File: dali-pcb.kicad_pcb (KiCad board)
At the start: 2 copper layers, 180.3 x 106.7 mm, 57 parts, among them J1 12-22.5V DC, J10 LOLIN-S3 (R), J11 ESP32-S3-DEVKITC-1 (L), J12 ESP32-S3-DEVKITC-1 (R), J13 LOLIN-S2-MINI (L), J14 LOLIN-S2-MINI (R), J15 DALI BUS, J16 DALI BUS, J17 FTDI-MCU, J18 A10, J19 A5-1, J2 DALI BUS, J20 A5-2, J21 A2-1, J22 A2-2, J23 A2-3, J24 A2-4, J25 A2-5, J26 D8, J27 D4-1, J28 D4-2, J29 D2-1, J3 5V DC, J30 D2-2, J31 D2-3, J32 D2-4, J33 D1-11, J34 D1-12, J35 D1-13, J36 D1-14, J37 FTDI-DALI, J4 5V DC, J5 5V DC, J6 5V DC, J7 5V DC, J8 GND, J9 LOLIN-S3 (L), Q1 PZT2222A, Q2 MMBT2222A, U1 TCLT1000, U2 TCLT1000

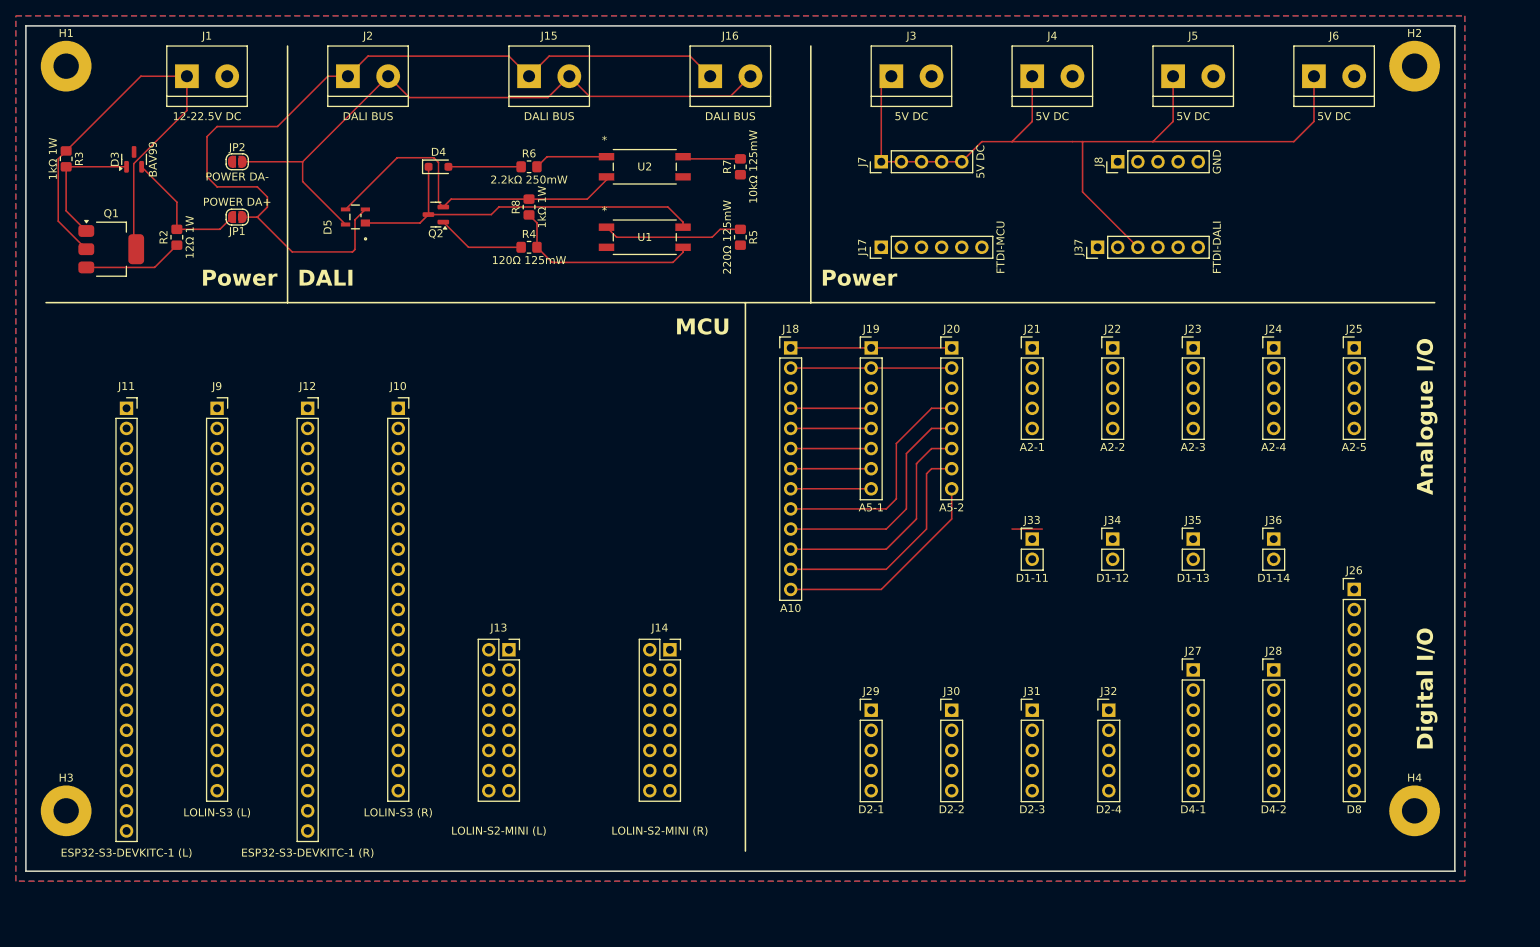
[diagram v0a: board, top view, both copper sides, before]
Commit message: Increase board size to protect the MCU USB connections
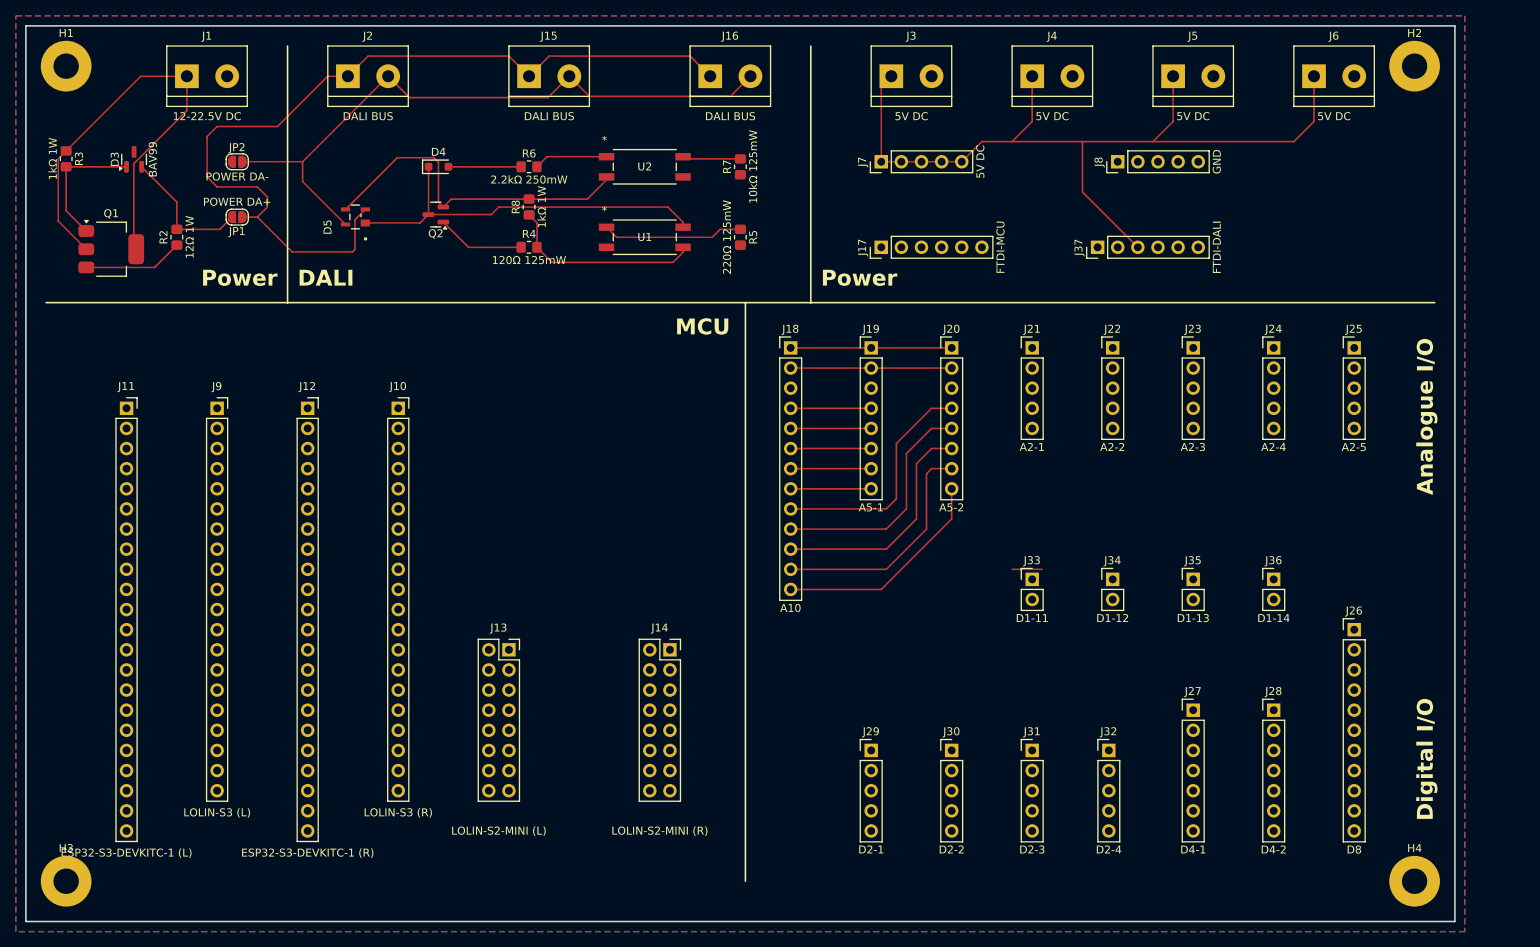
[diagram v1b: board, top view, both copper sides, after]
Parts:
- moved H3 8.89 mm to (20.3, 123.2)
- moved H4 8.89 mm to (190.5, 123.2)
- moved J29 5.08 mm to (121.9, 106.7)
- moved J30 5.08 mm to (132.1, 106.7)
- moved J31 5.08 mm to (142.2, 106.7)
- moved J32 5.08 mm to (151.9, 106.7)
- moved J26 5.08 mm to (182.9, 91.4)
- moved J27 5.08 mm to (162.6, 101.6)
- moved J28 5.08 mm to (172.7, 101.6)
- moved J33 5.08 mm to (142.2, 85.1)
- moved J34 5.08 mm to (152.4, 85.1)
- moved J35 5.08 mm to (162.6, 85.1)
- moved J36 5.08 mm to (172.7, 85.1)
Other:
- board size 180.3 x 106.7 mm -> 180.3 x 113 mm
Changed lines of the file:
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@@
 	(footprint "Connector_PinHeader_2.54mm:PinHeader_1x05_P2.54mm_Vertical"
 		(layer "F.Cu")
-		(at 151.91 101.6)
+		(at 151.91 106.68)
 		(descr "Through hole straight pin header, 1x05, 2.54mm pitch, single row")
 		(tags "Through hole pin header THT 1x05 2.54mm single row")
@@
 	(footprint "Connector_PinHeader_2.54mm:PinHeader_1x02_P2.54mm_Vertical"
 		(layer "F.Cu")
-		(at 162.56 80.01)
+		(at 162.56 85.09)
 		(descr "Through hole straight pin header, 1x02, 2.54mm pitch, single row")
 		(tags "Through hole pin header THT 1x02 2.54mm single row")
@@
 	(footprint "Connector_PinHeader_2.54mm:PinHeader_1x07_P2.54mm_Vertical"
 		(layer "F.Cu")
-		(at 162.56 96.52)
+		(at 162.56 101.6)
 		(descr "Through hole straight pin header, 1x07, 2.54mm pitch, single row")
 		(tags "Through hole pin header THT 1x07 2.54mm single row")
@@
 	(footprint "Connector_PinHeader_2.54mm:PinHeader_1x05_P2.54mm_Vertical"
 		(layer "F.Cu")
-		(at 142.24 101.6)
+		(at 142.24 106.68)
 		(descr "Through hole straight pin header, 1x05, 2.54mm pitch, single row")
 		(tags "Through hole pin header THT 1x05 2.54mm single row")
@@
 	(footprint "Connector_PinHeader_2.54mm:PinHeader_1x07_P2.54mm_Vertical"
 		(layer "F.Cu")
-		(at 172.72 96.52)
+		(at 172.72 101.6)
 		(descr "Through hole straight pin header, 1x07, 2.54mm pitch, single row")
 		(tags "Through hole pin header THT 1x07 2.54mm single row")
@@
 	(footprint "Connector_PinHeader_2.54mm:PinHeader_1x02_P2.54mm_Vertical"
 		(layer "F.Cu")
-		(at 172.72 80.01)
+		(at 172.72 85.09)
 		(descr "Through hole straight pin header, 1x02, 2.54mm pitch, single row")
 		(tags "Through hole pin header THT 1x02 2.54mm single row")
@@
 	(footprint "Connector_PinHeader_2.54mm:PinHeader_1x02_P2.54mm_Vertical"
 		(layer "F.Cu")
-		(at 142.24 80.01)
+		(at 142.24 85.09)
 		(descr "Through hole straight pin header, 1x02, 2.54mm pitch, single row")
 		(tags "Through hole pin header THT 1x02 2.54mm single row")
@@
 	(footprint "Connector_PinHeader_2.54mm:PinHeader_1x05_P2.54mm_Vertical"
 		(layer "F.Cu")
-		(at 132.08 101.6)
+		(at 132.08 106.68)
 		(descr "Through hole straight pin header, 1x05, 2.54mm pitch, single row")
 		(tags "Through hole pin header THT 1x05 2.54mm single row")
@@
 	(footprint "Connector_PinHeader_2.54mm:PinHeader_1x02_P2.54mm_Vertical"
 		(layer "F.Cu")
-		(at 152.4 80.01)
+		(at 152.4 85.09)
 		(descr "Through hole straight pin header, 1x02, 2.54mm pitch, single row")
 		(tags "Through hole pin header THT 1x02 2.54mm single row")
@@
 	(footprint "MountingHole:MountingHole_3.2mm_M3_Pad"
 		(layer "F.Cu")
-		(at 190.5 114.3)
+		(at 190.5 123.19)
 		(descr "Mounting Hole 3.2mm, M3, generated by kicad-footprint-generator mountinghole.py")
 		(tags "mountinghole M3")
@@
 	(footprint "MountingHole:MountingHole_3.2mm_M3_Pad"
 		(layer "F.Cu")
-		(at 20.32 114.3)
+		(at 20.32 123.19)
 		(descr "Mounting Hole 3.2mm, M3, generated by kicad-footprint-generator mountinghole.py")
 		(tags "mountinghole M3")
@@
 	(footprint "Connector_PinHeader_2.54mm:PinHeader_1x05_P2.54mm_Vertical"
 		(layer "F.Cu")
-		(at 121.92 101.6)
+		(at 121.92 106.68)
 		(descr "Through hole straight pin header, 1x05, 2.54mm pitch, single row")
 		(tags "Through hole pin header THT 1x05 2.54mm single row")
@@
 	(footprint "Connector_PinHeader_2.54mm:PinHeader_1x11_P2.54mm_Vertical"
 		(layer "F.Cu")
-		(at 182.88 86.36)
+		(at 182.88 91.44)
 		(descr "Through hole straight pin header, 1x11, 2.54mm pitch, single row")
 		(tags "Through hole pin header THT 1x11 2.54mm single row")
@@
 	(gr_line
 		(start 106.045 50.165)
-		(end 106.045 119.38)
+		(end 106.045 123.19)
 		(stroke
 			(width 0.2)
@@
 	(gr_rect
 		(start 15.24 15.24)
-		(end 195.58 121.92)
+		(end 195.58 128.27)
 		(stroke
 			(width 0.2)
@@
 	)
 	(gr_text "Digital I/O"
-		(at 193.04 106.68 90)
+		(at 193.04 115.57 90)
 		(layer "F.SilkS")
 		(effects
@@
 		(layer "Cmts.User")
 		(pts
+			(xy 27.94 118.17) (xy 27.94 128.27)
+		)
+		(height -19.05)
+		(orientation 1)
+		(format
+			(prefix "")
+			(suffix "")
+			(units 2)
+			(units_format 1)
+			(precision 4)
+			(suppress_zeroes yes)
+		)
+		(style
+			(thickness 0.1)
+			(arrow_length 1.27)
+			(text_position_mode 0)
+			(arrow_direction outward)
+			(extension_height 0.58642)
+			(extension_offset 0.5)
+			(keep_text_aligned yes)
+		)
+		(gr_text "10.1 mm"
+			(at 7.79 123.22 90)
+			(layer "Cmts.User")
+			(effects
+				(font
+					(size 1 1)
+					(thickness 0.1)
+				)
+			)
+		)
+	)
+	(dimension
+		(type orthogonal)
+		(layer "Cmts.User")
+		(pts
 			(xy 62.23 111.76) (xy 73.66 111.76)
 		)
@@
 	)
 	(segment
-		(start 143.51 78.74)
-		(end 139.7 78.74)
+		(start 143.51 83.82)
+		(end 139.7 83.82)
 		(width 0.2)
 		(layer "F.Cu")
@@
 		(min_thickness 0.25)
 		(filled_areas_thickness no)
-		(fill yes
+		(fill
 			(thermal_gap 0.5)
 			(thermal_bridge_width 0.5)
@@
 		(polygon
 			(pts
-				(xy 13.97 13.97) (xy 196.85 13.97) (xy 196.85 123.19) (xy 13.97 123.19)
+				(xy 13.97 13.97) (xy 196.85 13.97) (xy 196.85 129.54) (xy 13.97 129.54)
 			)
 		)

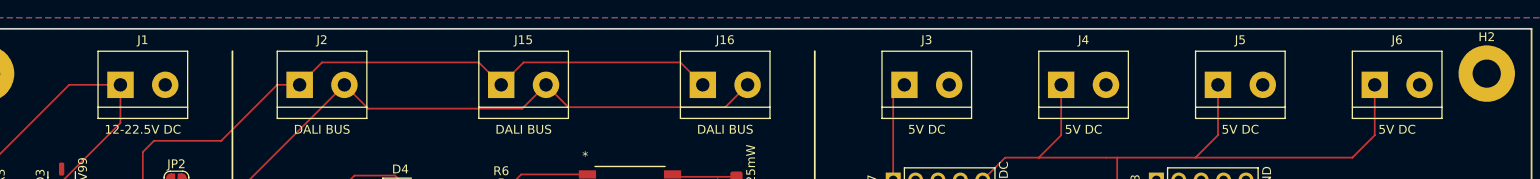
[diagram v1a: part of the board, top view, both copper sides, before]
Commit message: Add +/- labels to screw terminals
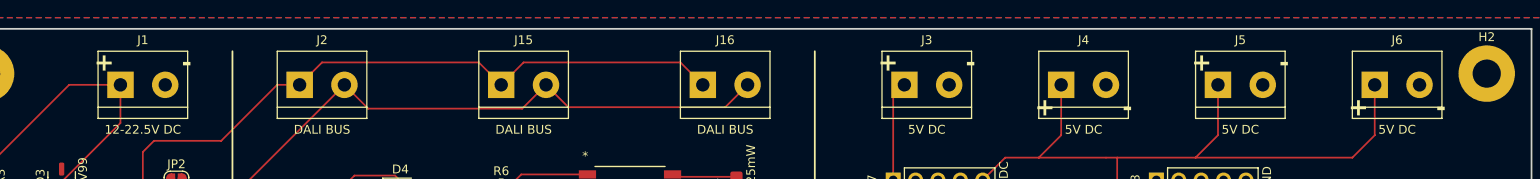
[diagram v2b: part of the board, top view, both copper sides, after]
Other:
- board text added: "+ -"
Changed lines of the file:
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@@
+		)
+	)
+	(gr_text "+        -"
+		(at 127 19.05 0)
+		(layer "F.SilkS")
+		(effects
+			(font
+				(size 2 2)
+				(thickness 0.4)
+				(bold yes)
+			)
+		)
+	)
+	(gr_text "+        -"
+		(at 144.78 24.13 0)
+		(layer "F.SilkS")
+		(effects
+			(font
+				(size 2 2)
+				(thickness 0.4)
+				(bold yes)
+			)
+		)
+	)
+	(gr_text "+        -"
+		(at 162.56 19.05 0)
+		(layer "F.SilkS")
+		(effects
+			(font
+				(size 2 2)
+				(thickness 0.4)
+				(bold yes)
+			)
 		)
 	)
@@
 		)
 	)
+	(gr_text "+        -"
+		(at 180.34 24.13 0)
+		(layer "F.SilkS")
+		(effects
+			(font
+				(size 2 2)
+				(thickness 0.4)
+				(bold yes)
+			)
+		)
+	)
 	(gr_text "Analogue I/O"
 		(at 193.04 54.61 90)
@@
 			)
 			(justify left bottom)
+		)
+	)
+	(gr_text "+        -"
+		(at 38.1 19.05 0)
+		(layer "F.SilkS")
+		(effects
+			(font
+				(size 2 2)
+				(thickness 0.4)
+				(bold yes)
+			)
 		)
 	)
@@
 		(min_thickness 0.25)
 		(filled_areas_thickness no)
-		(fill
+		(fill yes
 			(thermal_gap 0.5)
 			(thermal_bridge_width 0.5)

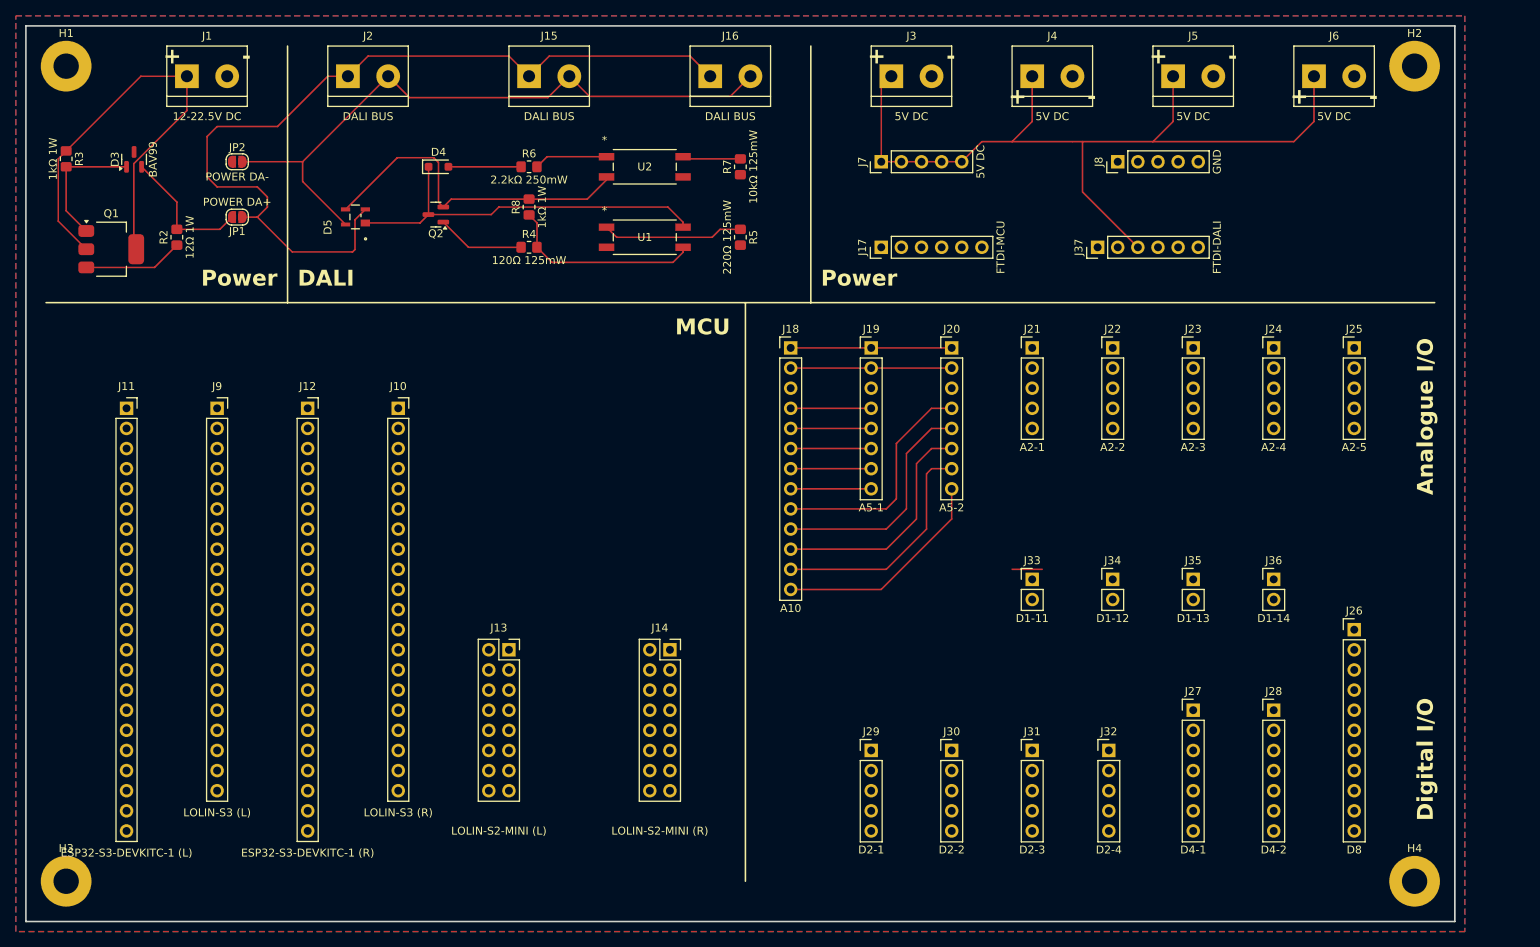
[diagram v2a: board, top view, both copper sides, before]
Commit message: FTDI TTL-232R-3V3 can't be used to directly interface with DALI
There's no 3.3V supply to use as a pull-up
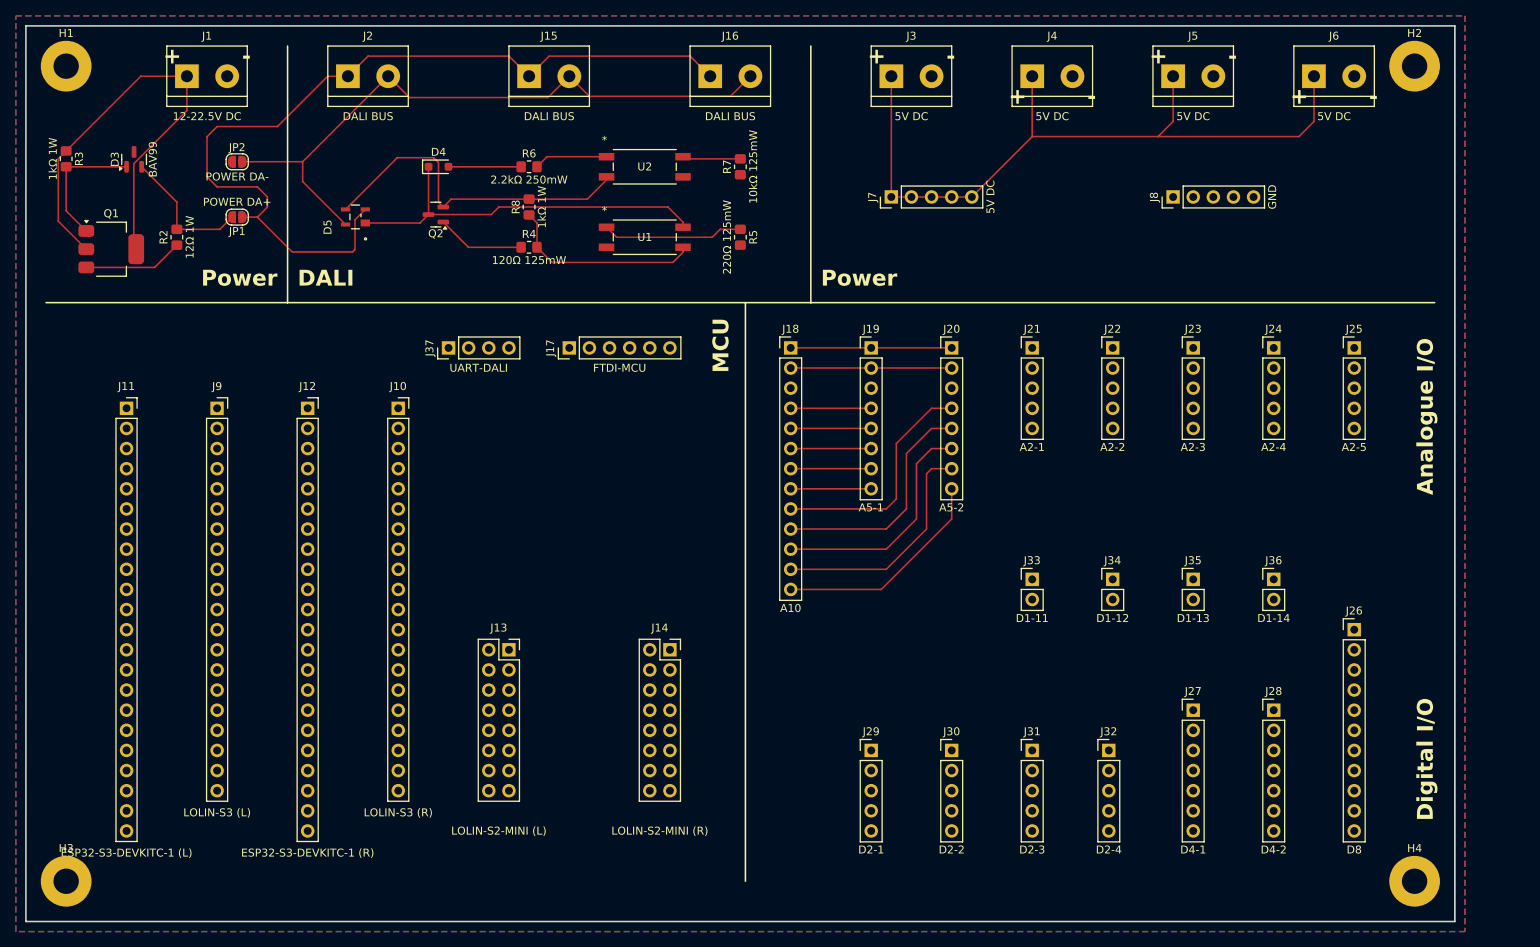
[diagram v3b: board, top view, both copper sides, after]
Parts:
- J37: value FTDI-DALI -> UART-DALI; footprint Connector_PinHeader_2.54mm:PinHeader_1x06_P2.54mm_Vertical -> Connector_PinHeader_2.54mm:PinHeader_1x04_P2.54mm_Vertical
- moved J37 82.9 mm to (68.6, 55.9)
- moved J17 41.4 mm to (83.8, 55.9)
- moved J8 8.28 mm to (160.0, 36.8)
- moved J7 4.62 mm to (124.5, 36.8)
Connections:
- J37 pad 1: GND -> +3.3V
- J37 pad 2: unconnected-(J37-Pin_2-Pad2) -> /DALI/DALI_RX
- J37 pad 3: +5V -> /DALI/DALI_TX
- J37 pad 4: /DALI/DALI_TX -> GND
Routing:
- net +5V: track 128.9 -> 114.6 mm
- net /IO/IO_A9: track 31.6 -> 27.8 mm
- net Net-(R5-Pad1): track 18.5 -> 17.8 mm
